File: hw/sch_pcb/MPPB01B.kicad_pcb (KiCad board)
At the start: 2 copper layers, 101.1 x 101.1 mm, 28 parts, among them P1 BTH-030-01-F-D-A, P10 SATA7-67491-1030, P11 HEADER_2x05_PARALLEL, P12 HEADER_2x05_PARALLEL, P2 BTH-030-01-F-D-A, P3 BTH-030-01-F-D-A, P4 BTH-030-01-F-D-A, P5 SAS_mini_1888174-6, P6 SAS_mini_1888174-6, P7 HEADER_2x16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

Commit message: Edit bom and footprint
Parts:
- C2: value 100uF/10V -> 100uF/6V3
- C3, C4: footprint Capacitor_SMD:C_0805_2012Metric_Pad1.18x1.45mm_HandSolder -> Capacitor_SMD:C_0805_2012Metric

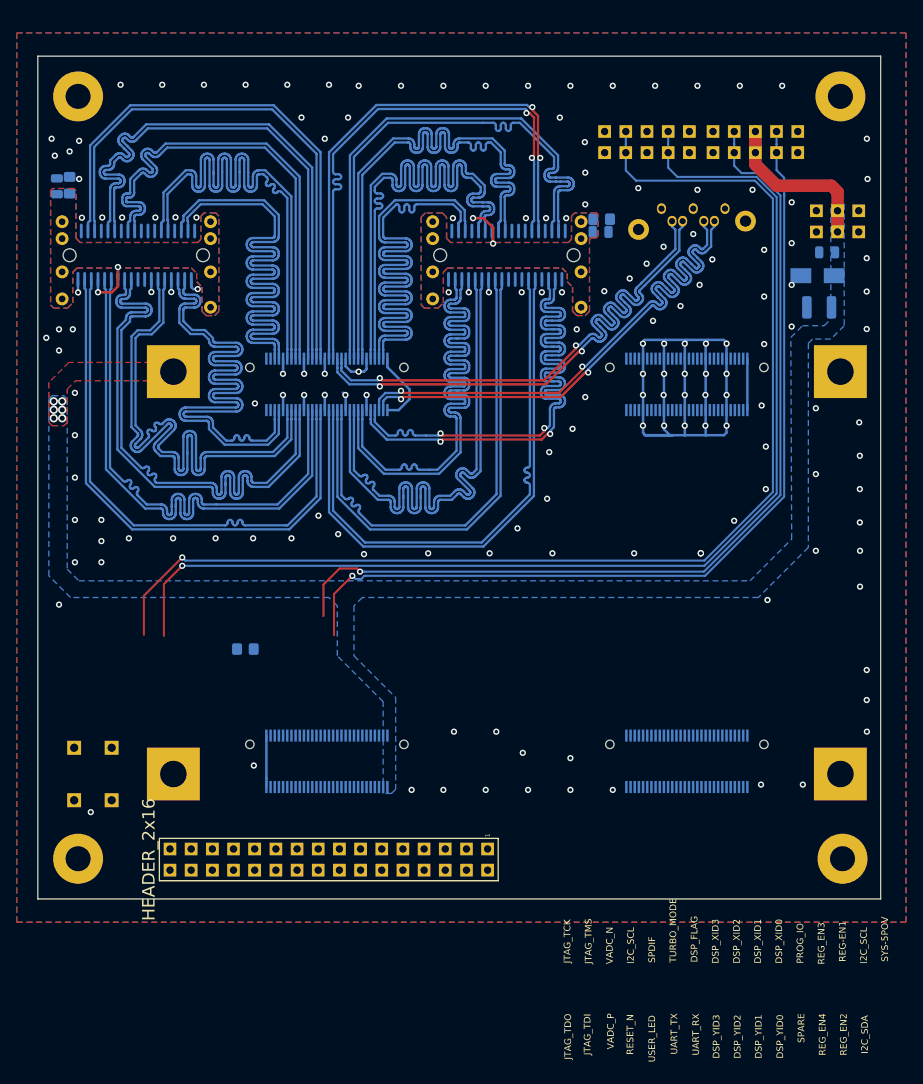
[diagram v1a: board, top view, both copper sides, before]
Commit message: Improve connector pinout #2
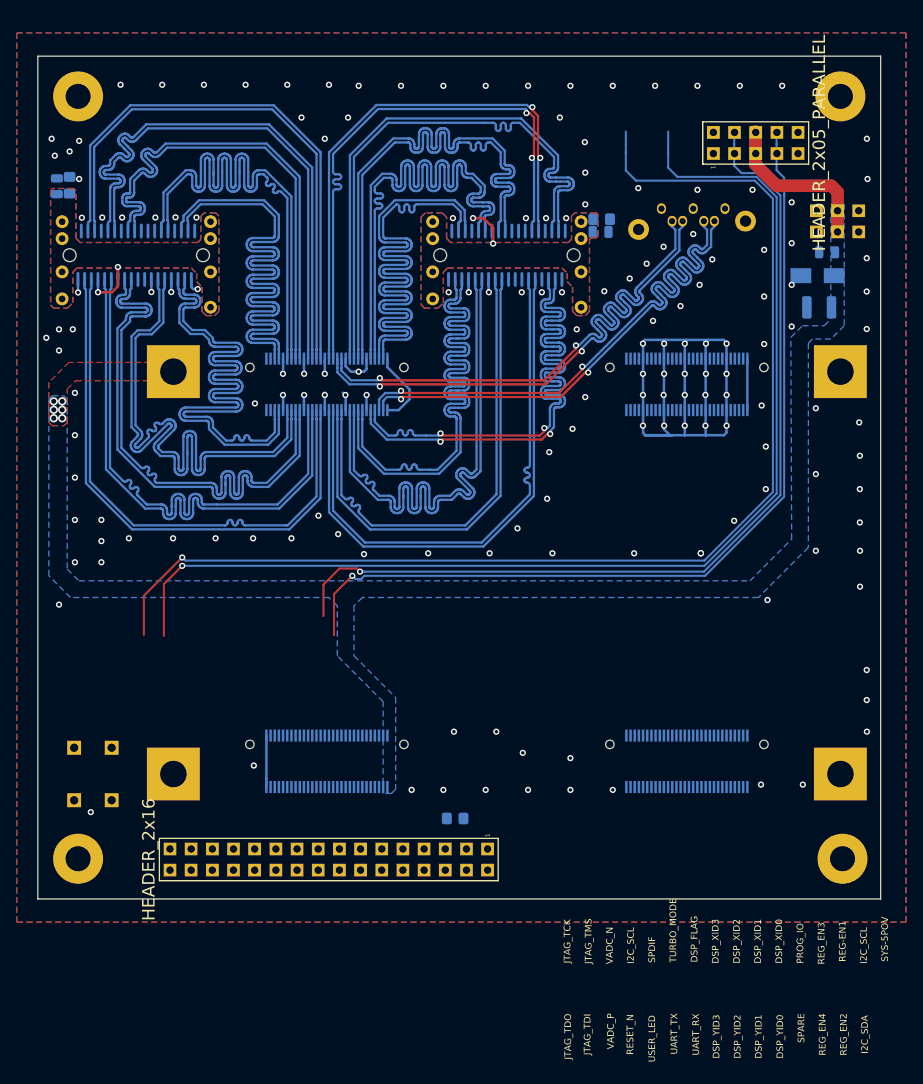
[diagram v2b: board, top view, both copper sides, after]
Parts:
- removed P12: HEADER_2x05_PARALLEL, Mlab_Pin_Headers:Straight_2x05
- P11: moved to F.Cu
- moved R3 32.3 mm to (157.0, 183.1), turned to 0 degrees
- moved P11 0.12 mm to (193.0, 102.1), turned to 90 degrees
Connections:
- P11 pad 5: /SYS-5POV -> /POWER/SYS-5POV
- P11 pad 6: /SYS-5POV -> /POWER/SYS-5POV
- P3 pad 10: /SPARE -> unconnected-(P3-Pad10)
- P7 pad 10: /SPARE -> /POWER/SPARE
- P7 pad 12: unconnected-(P7-Pad12) -> /2P5V
- P7 pad 14: unconnected-(P7-Pad14) -> /VDD_ADJ
- P7 pad 16: unconnected-(P7-Pad16) -> /VDD_GPIO
- P7 pad 3: /I2C_SCL -> /UART_RX
- P7 pad 4: /I2C_SDA -> /UART_TX
- P7 pad 5: /REG_EN1 -> GND
- P7 pad 6: /REG_EN2 -> /3P3V

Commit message: routing cest ke konektoru
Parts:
- added G***: LOGO, MLAB_LOGA:UST, F.Cu at (189.7, 186.7)
- moved R3 2.05 mm to (155.0, 183.5)
- moved C3 0.22 mm to (174.6, 112.9)
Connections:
- P7 pad 19: /DSP_FLAG -> /JTAG_TCK
- P7 pad 21: /TURBO_MODE -> /VADC_N
- P7 pad 23: /SPDIF -> /JTAG_TMS
- P7 pad 27: /VADC_N -> /SPDIF
- P7 pad 29: /JTAG_TMS -> /TURBO_MODE
- P7 pad 31: /JTAG_TCK -> /DSP_FLAG
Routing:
- net /UART_TX: track 144.5 -> 22.5 mm, vias 1 -> 0
- net /UART_RX: track 138.6 -> 19.3 mm, vias 1 -> 0
- net /RESET_N: track 0.00 -> 63.5 mm, vias 0 -> 1
- net /VDD_ADJ: track 0.00 -> 44.2 mm, vias 0 -> 2
- net /TURBO_MODE: track 0.00 -> 39.3 mm
- net /JTAG_TDI: track 0.00 -> 36.0 mm, vias 0 -> 1
- net /DSP_FLAG: track 0.00 -> 35.8 mm
- net /SPDIF: track 0.00 -> 31.3 mm
- net /JTAG_TCK: track 0.00 -> 30.3 mm
- net /JTAG_BOOT_EN: track 0.00 -> 29.3 mm
- net /JTAG_TDO: track 0.00 -> 28.3 mm, vias 0 -> 1
- net /JTAG_TMS: track 0.00 -> 28.2 mm
- net /3P3V: track 6.17 -> 34.3 mm, vias 0 -> 1
- net /2P5V: track 0.00 -> 26.1 mm, vias 0 -> 1
- net /VDD_GPIO: track 0.00 -> 22.5 mm, vias 0 -> 1
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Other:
- board text added: "MPPB01A MLAB, 2022"

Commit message: presun hrebinku
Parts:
- removed G***: LOGO, MLAB_LOGA:UST
- moved P11 88.6 mm to (171.5, 188.0), turned to -90 degrees
- moved P9 78.6 mm to (184.7, 188.0)
- moved D1 70.8 mm to (192.1, 188.3), turned to -90 degrees
- moved C1 68.8 mm to (195.9, 183.8), turned to 90 degrees
- moved C2 66.4 mm to (195.9, 188.1), turned to -90 degrees
- moved P7 0.06 mm to (141.8, 188.0)
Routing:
- net /I2C_SCL: track 131.5 -> 37.6 mm
- net /I2C_SDA: track 130.4 -> 37.8 mm
- net /SYS-5POV: track 25.1 -> 51.0 mm, vias 6 -> 14
- net /REG_EN4: track 16.5 -> 17.8 mm
- net /RESET_N: track 63.5 -> 64.1 mm
- net GND: vias 174 -> 171

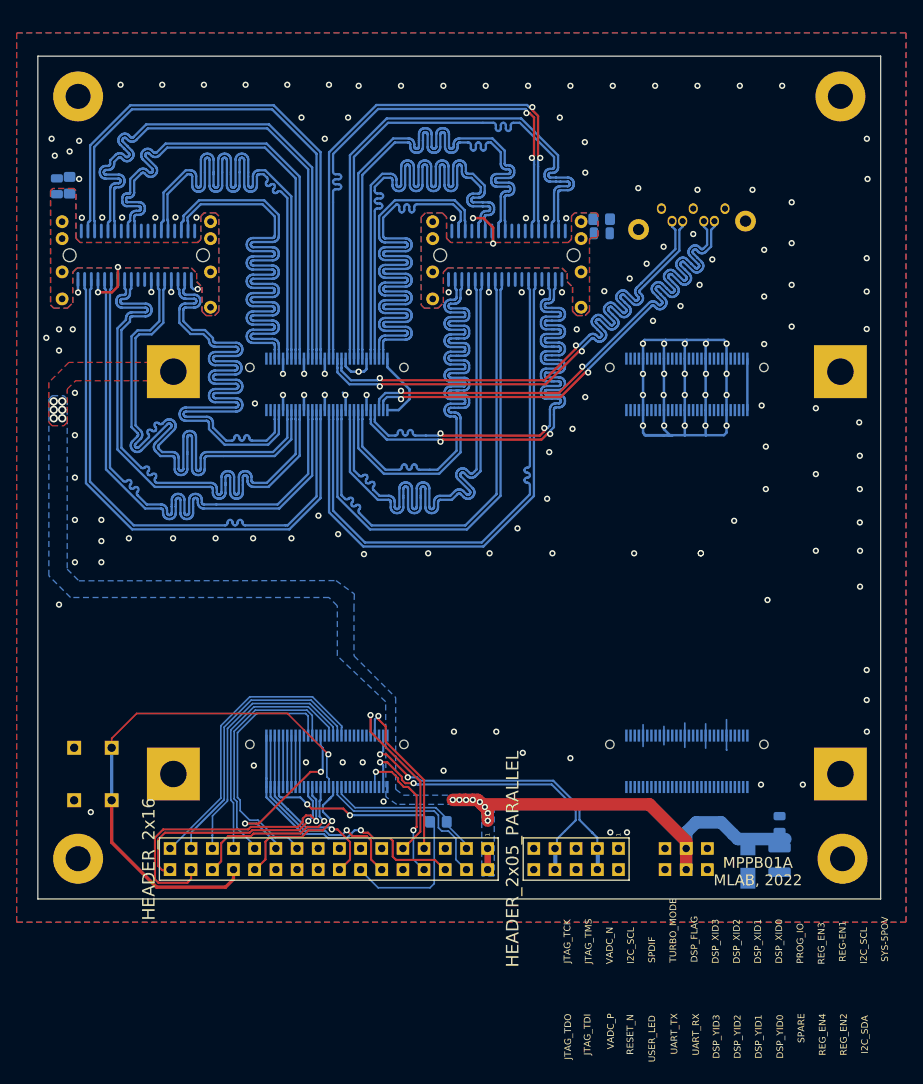
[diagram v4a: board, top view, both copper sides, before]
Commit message: uprava pinoutu konektoru
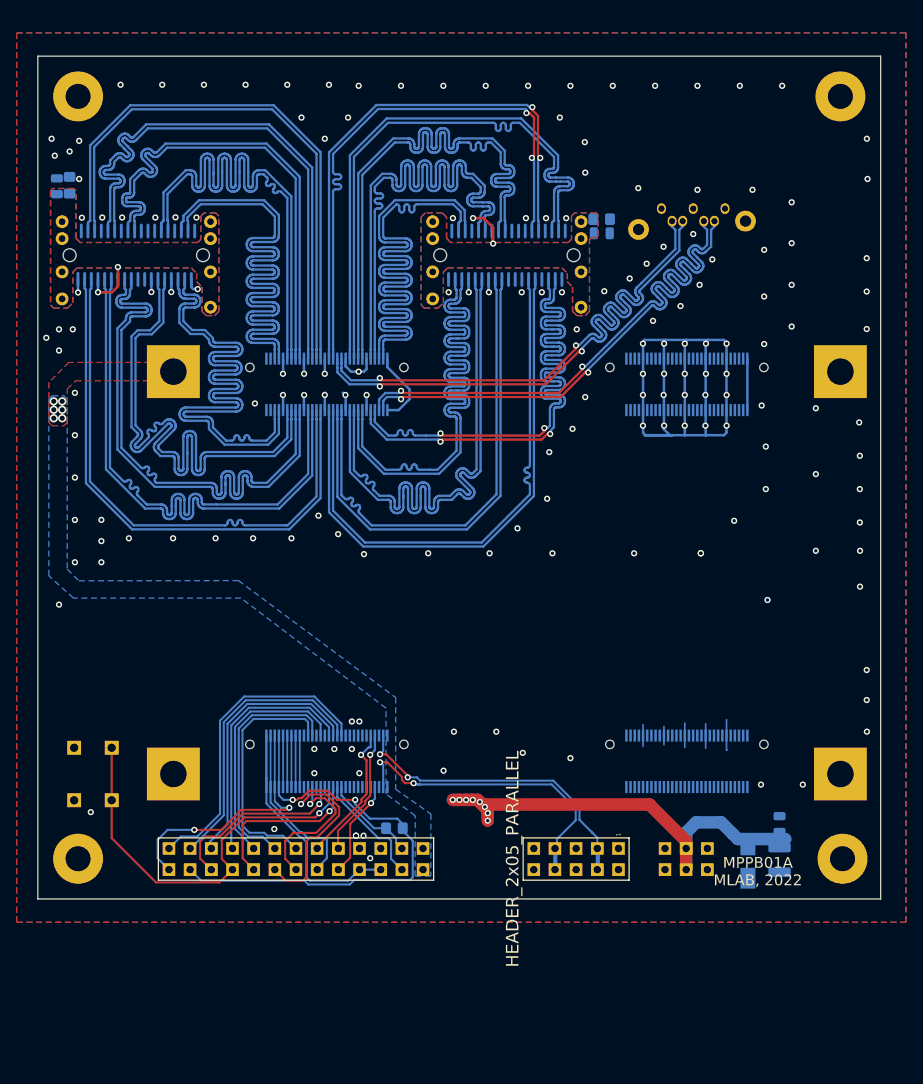
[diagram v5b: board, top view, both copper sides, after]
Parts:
- P7: value HEADER_2x16 -> HEADER_2x13; footprint Mlab_Pin_Headers:Straight_2x16 -> Mlab_Pin_Headers:Straight_2x13
- moved R3 5.33 mm to (149.7, 184.3), turned to 180 degrees
- moved P7 3.93 mm to (137.9, 188.0)
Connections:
- P7 pad 10: /POWER/SPARE -> /REG_EN4
- P7 pad 11: unconnected-(P7-Pad11) -> /PROG_IO
- P7 pad 13: unconnected-(P7-Pad13) -> /JTAG_TCK
- P7 pad 14: /VDD_ADJ -> /JTAG_TDI
- P7 pad 15: unconnected-(P7-Pad15) -> /JTAG_TMS
- P7 pad 16: /VDD_GPIO -> /JTAG_TDO
- P7 pad 17: unconnected-(P7-Pad17) -> /VADC_N
- P7 pad 18: unconnected-(P7-Pad18) -> /USER_LED
- P7 pad 19: /JTAG_TCK -> /JTAG_BOOT_EN
- P7 pad 20: unconnected-(P7-Pad20) -> /RESET_N
- P7 pad 21: /VADC_N -> /SPDIF
- P7 pad 22: unconnected-(P7-Pad22) -> /VADC_P
- P7 pad 23: /JTAG_TMS -> /TURBO_MODE
- P7 pad 24: /USER_LED -> /VDD_ADJ
- P7 pad 25: /JTAG_BOOT_EN -> /DSP_FLAG
- P7 pad 26: /RESET_N -> /VDD_GPIO
- P7 pad 7: /REG_EN3 -> GND
- P7 pad 8: /REG_EN4 -> /3P3V
- P7 pad 9: /PROG_IO -> /REG_EN3
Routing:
- net /JTAG_TDI: track 36.0 -> 17.9 mm
- net /VDD_ADJ: track 44.2 -> 59.4 mm
- net /RESET_N: track 64.1 -> 49.0 mm
- net /VDD_GPIO: track 22.5 -> 31.6 mm, vias 1 -> 2
- net /UART_TX: track 22.5 -> 13.8 mm
- net /UART_RX: track 19.3 -> 11.2 mm
- net /VADC_N: track 22.0 -> 28.5 mm, vias 2 -> 0
- net /REG_EN4: track 17.8 -> 11.7 mm, vias 2 -> 1
- net /3P3V: track 34.4 -> 28.7 mm, vias 1 -> 0
- net /2P5V: track 26.1 -> 20.7 mm, vias 1 -> 0
- net /REG_EN3: track 20.7 -> 15.4 mm
- net /TURBO_MODE: track 39.3 -> 34.1 mm
- net /JTAG_TDO: track 28.3 -> 23.1 mm
- net /PROG_IO: track 21.9 -> 16.9 mm
- net /POWER/SYS-5POV: track 2.54 -> 0.00 mm
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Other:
- board text added: "1"
- board text added: "1 SYS_5V 3 RX 5 GND 7 GND 9 REG_EN3 11 PROG_IO 13 JTAG_TCK 15 JTAG_TMS 17 VADC_N 19 JTAG_BOOT_EN 21 VADC_N 23 TURBO_MODE 25 DSP_FLAG"
- board text added: "10"
- board text added: "13"
- board text added: "14"
- board text added: "17"
- board text added: "18"
- board text added: "2"
- board text added: "21"
- board text added: "22"
- board text added: "25"
- board text added: "26"
- board text added: "6"
- board text added: "9"
- board text added: "P7"
- board text added: "P7 Pinout"
- board text added: "PWR"
- board text added: "SYS 5V 2 TX 4 3p3V 6 3p3V 8 REG_EN4 10 2p5V 12 JTAG_TDI 14 JTAG_TDO 16 USER_LED 18 RESET_N 20 VADC_P 22 VDD_ADJ 24 VDD_GPIO 26"
- board text removed: "DSP_FLAG"
- board text removed: "DSP_XID0"
- board text removed: "DSP_XID1"
- board text removed: "DSP_XID2"
- board text removed: "DSP_XID3"
- board text removed: "DSP_YID0"
- board text removed: "DSP_YID1"
- board text removed: "DSP_YID2"
- board text removed: "DSP_YID3"
- board text removed: "JTAG_TCK"
- board text removed: "JTAG_TDI"
- board text removed: "JTAG_TDO"
- board text removed: "JTAG_TMS"
- board text removed: "PROG_IO"
- board text removed: "REG-EN1"
- board text removed: "REG_EN2"
- board text removed: "REG_EN3"
- board text removed: "REG_EN4"
- board text removed: "RESET_N"
- board text removed: "SPARE"
- board text removed: "SPDIF"
- board text removed: "SYS-5POV"
- board text removed: "TURBO_MODE"
- board text removed: "UART"
- board text removed: "USER_LED"
- board text removed: "VADC_N"
- board text removed: "VADC_P"
